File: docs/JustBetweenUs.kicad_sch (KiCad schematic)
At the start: 39 parts, among them J10 AudioJack, J11 AudioJack, J12 AudioJack, J13 AudioJack, J5 PwrHeader, J6 EurorackPwr, SW3 SW_Push, U3 LM1117T-5.0, U4 TL074

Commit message: cleanup kicad file
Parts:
- removed J10, J11: AudioJack, symbol Connector_Audio:AudioJack2_Ground
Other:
- removed sheet Output 1
- removed sheet Output 2
- removed sheet old

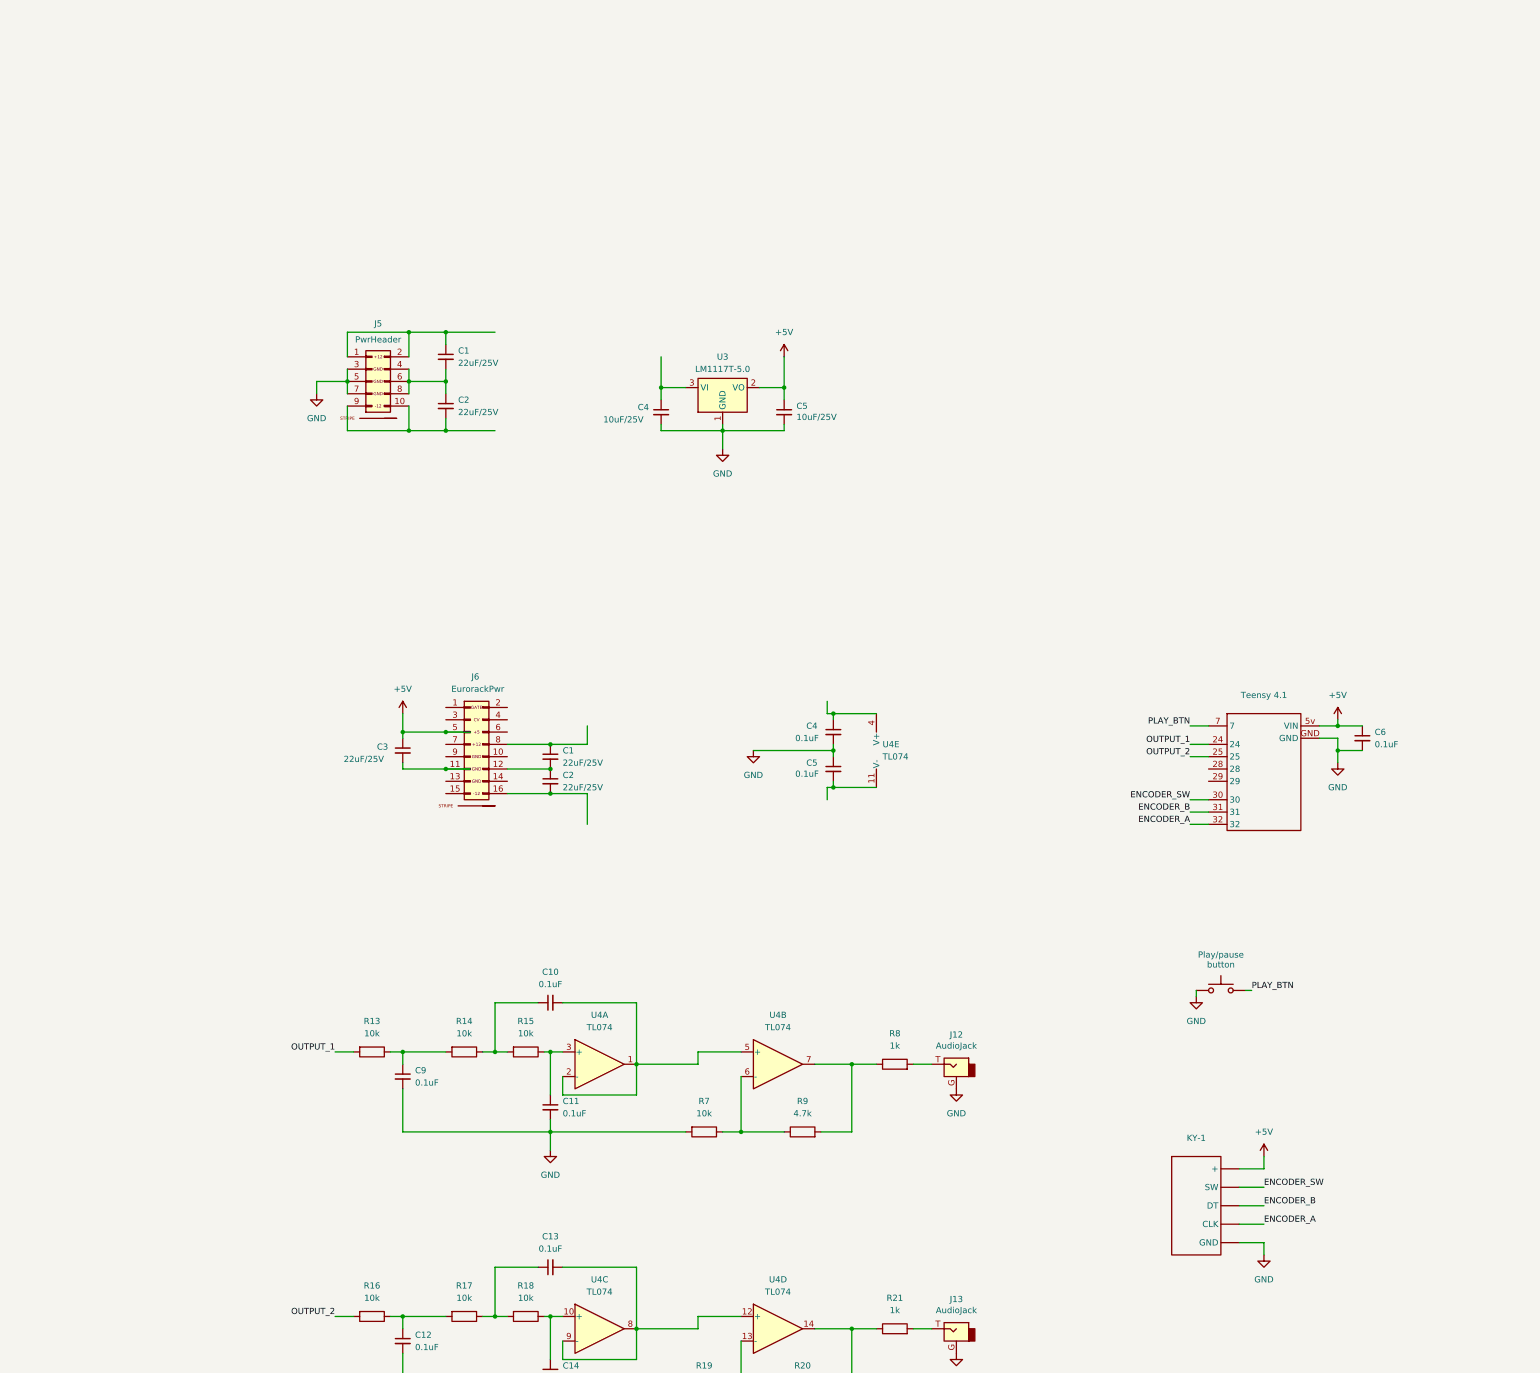
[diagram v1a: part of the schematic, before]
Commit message: Insert power layout by @8sevenCentral
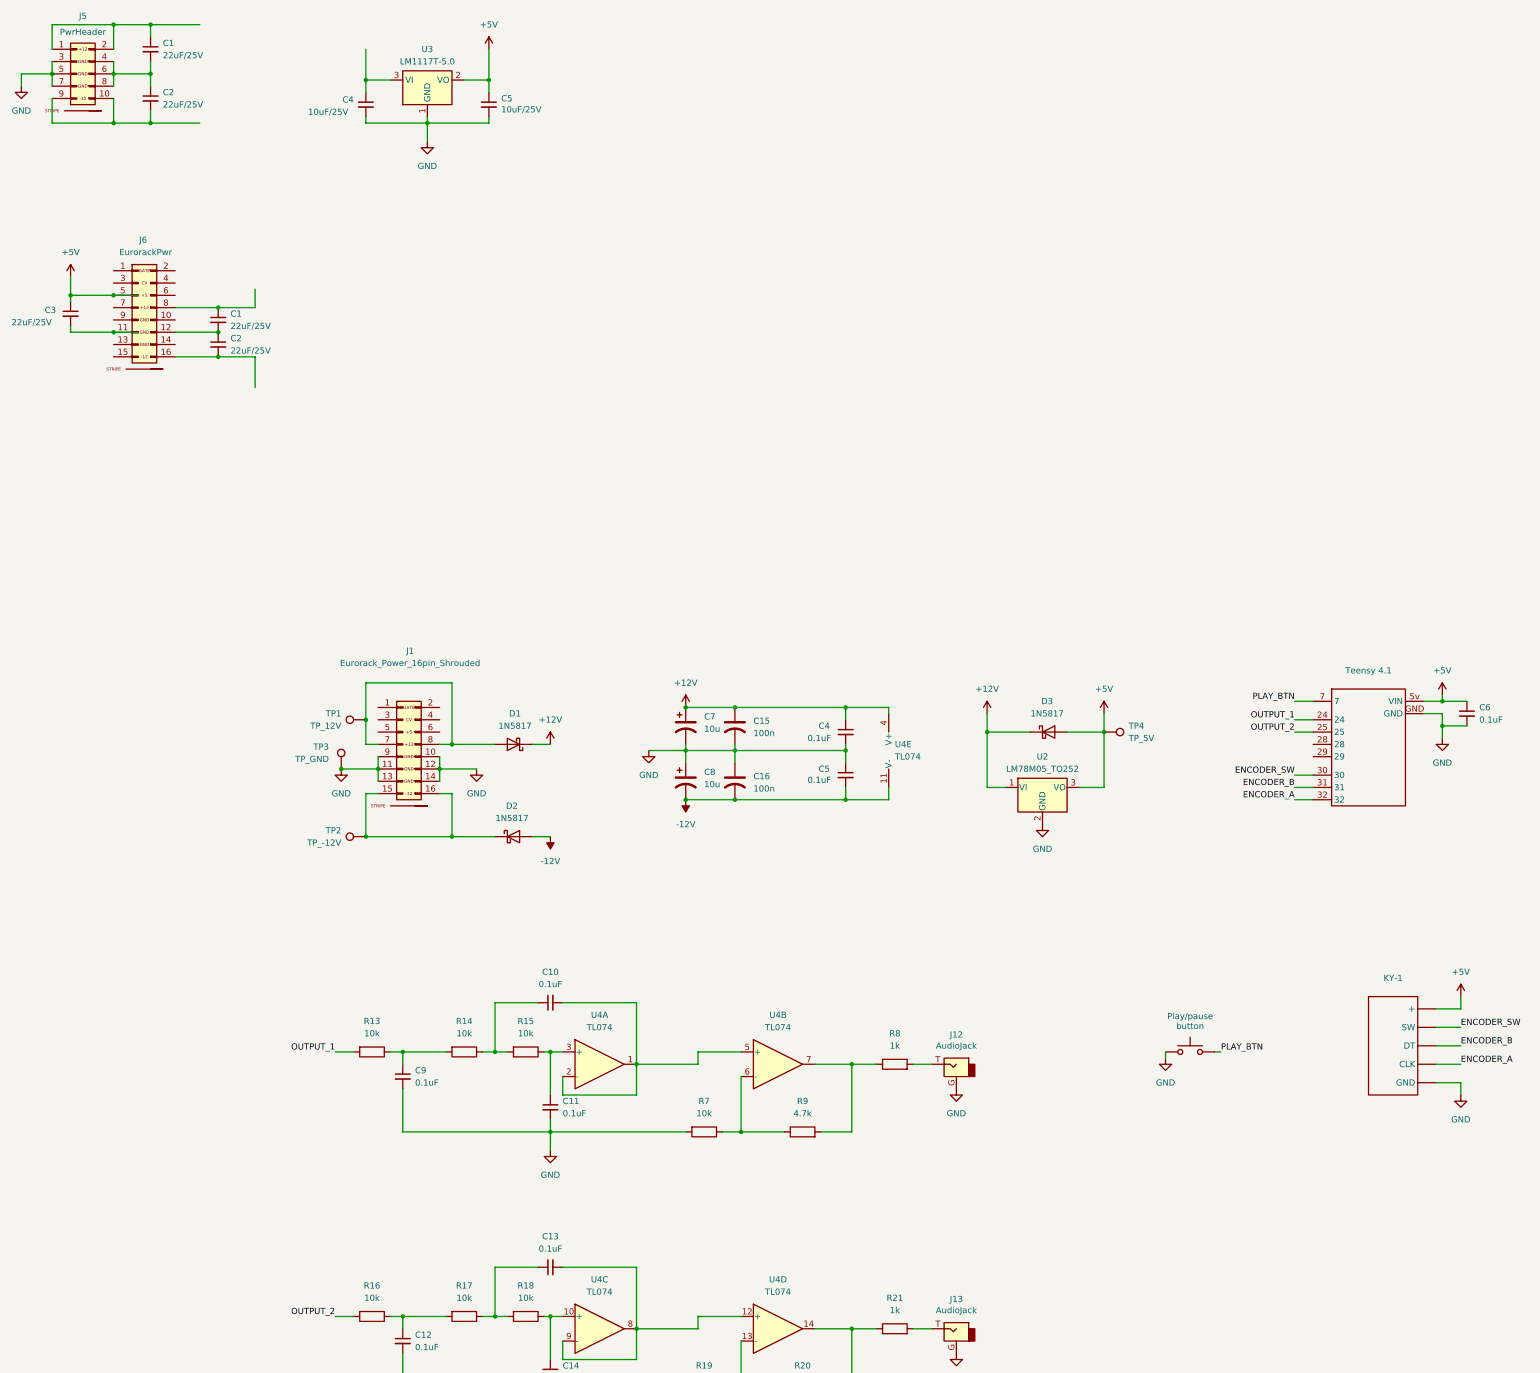
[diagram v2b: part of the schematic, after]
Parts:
- added C15, C16: 100n, symbol Device:C_US
- added C7, C8: 10u, symbol Device:C_Polarized_US
- added D1, D2, D3: 1N5817, Diode_THT:D_DO-41_SOD81_P10.16mm_Horizontal, symbol Diode:1N5817
- added J1: Eurorack_Power_16pin_Shrouded, 4ms_Connector:Pins_2x08_2.54mm_TH_EuroPower_Shrouded, symbol PCM_4ms_Connector:Eurorack_Power_16pin_Shrouded
- added TP1: TP_12V, TestPoint:TestPoint_Pad_D1.0mm, symbol Connector:TestPoint
- added TP2: TP_-12V, TestPoint:TestPoint_Pad_D1.0mm, symbol Connector:TestPoint
- added TP3: TP_GND, TestPoint:TestPoint_Pad_D1.0mm, symbol Connector:TestPoint
- added TP4: TP_5V, TestPoint:TestPoint_Pad_D1.0mm, symbol Connector:TestPoint
- added U2: LM78M05_TO252, Package_TO_SOT_SMD:TO-252-2, symbol Regulator_Linear:LM78M05_TO252
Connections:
- net +5V: now also D3.2 (A), TP4.1, U2.3 (VO)
- net GND: now also C15.2, C16.1, C7.2, C8.1, J1.10 (GND), J1.11 (GND), J1.12 (GND), J1.13 (-12), J1.14 (-12V), J1.9 (GND), TP3.1, U2.2 (GND)
- net -12V: now reaches C5.2, U4.11 (V-)
- net -12V: now also C16.2, C8.2, D2.2 (A)
- net +12V: now reaches C4.1, U4.4 (V+)
- net +12V: now also C15.1, C7.1, D1.1 (K), D3.1 (K), U2.1 (VI)
- new net: D2.1 (K), J1.15 (-12V), J1.16 (P16), TP2.1
- new net: D1.2 (A), J1.7 (12V), J1.8 (+12V), TP1.1
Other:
- moved on the sheet: C1, C2, C3, C4, C5, C6, J5, J6, KY-1, Teensy 4.1, U3, U4E
